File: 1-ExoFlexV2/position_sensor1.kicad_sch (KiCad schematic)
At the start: 28 parts, among them U51 SN74LVC1G08DBVR, U52 SN74LVC1G08DBVR, U53 SN74LVC3G14DCUT_V2

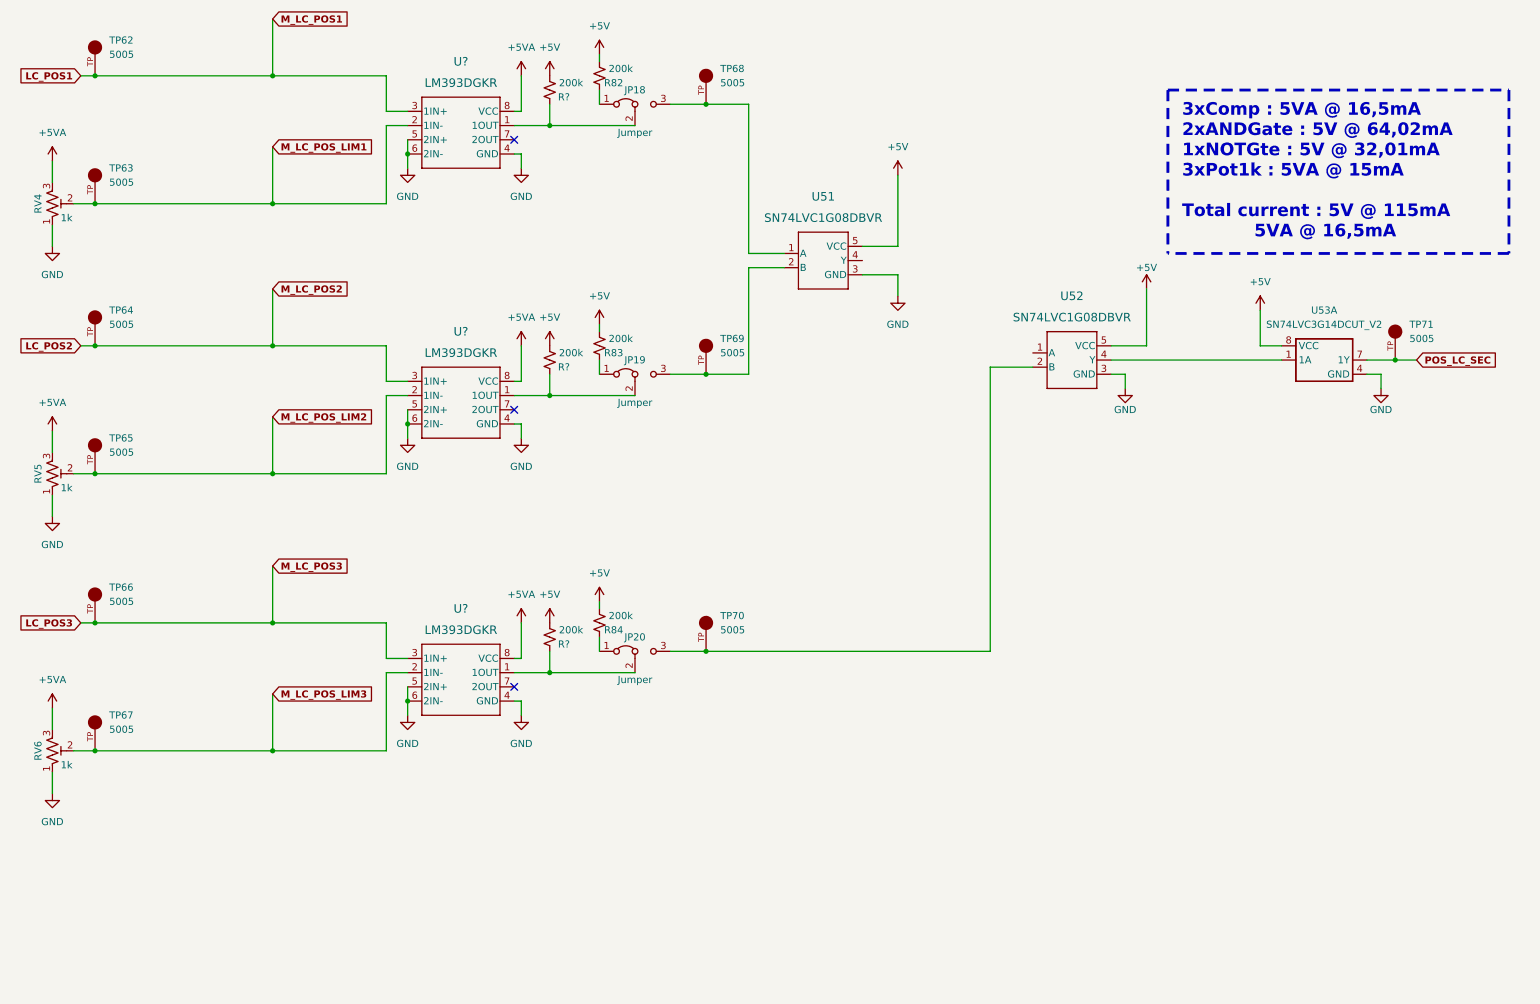
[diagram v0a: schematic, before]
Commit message: Chokes et RC
- Ajout des RF chokes
- Changement des résistance pour 0805
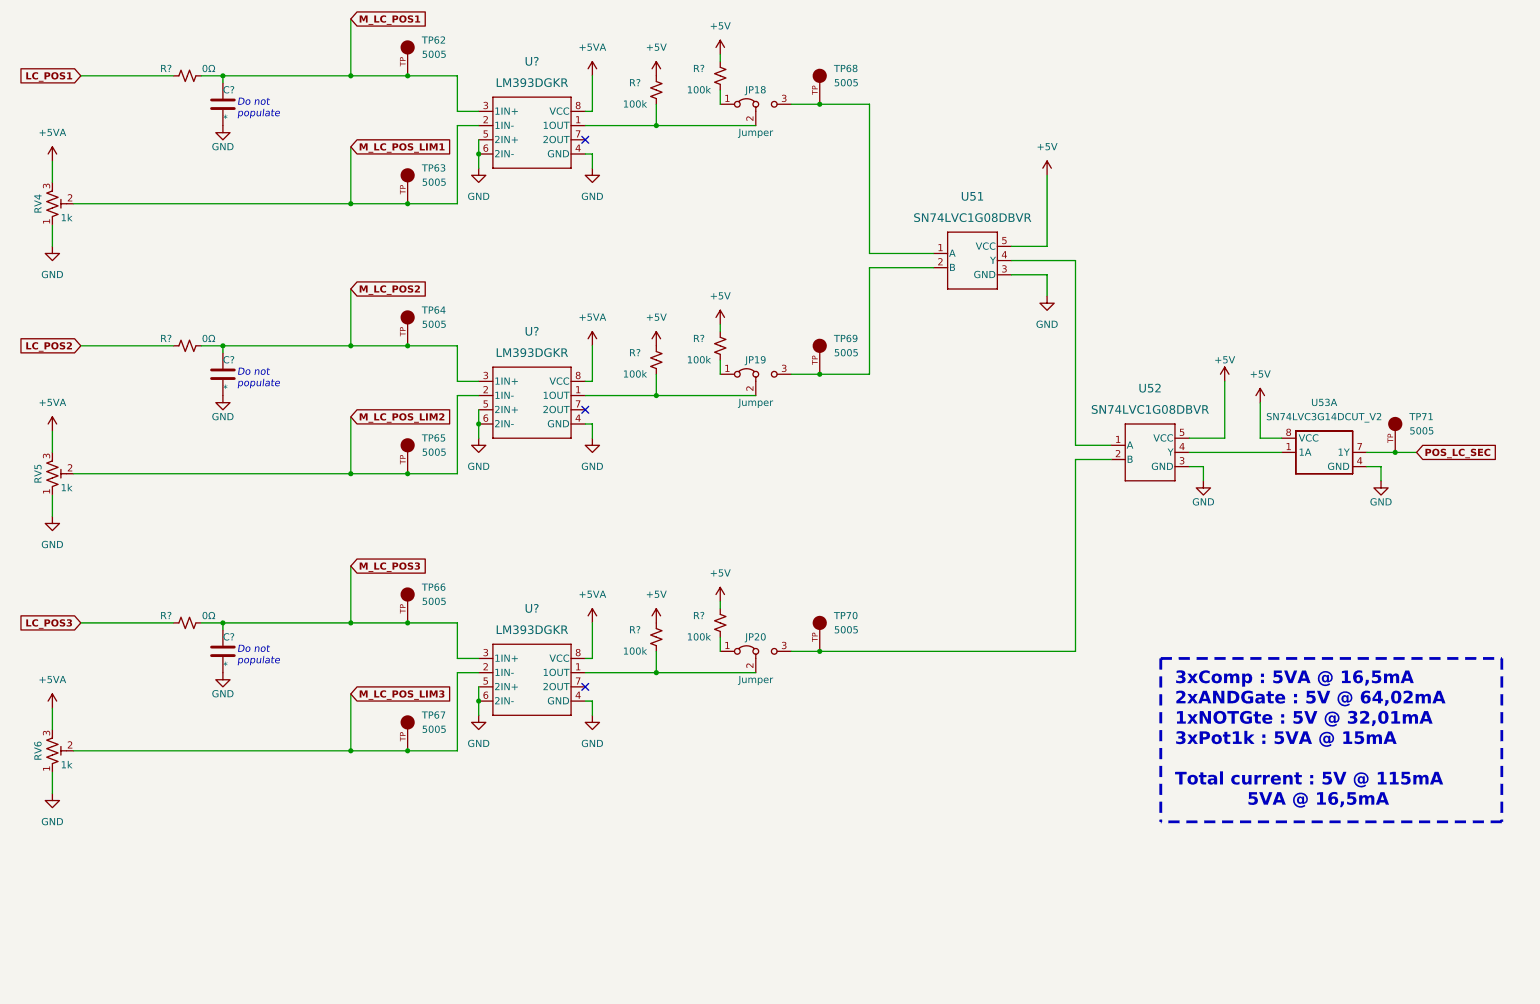
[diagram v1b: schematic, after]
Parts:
- removed R82, R83, R84, R? (x3): 200k, Resistor_SMD:R_0603_1608Metric, symbol Device:R_Small_US
- added C? (x3): *, Capacitor_SMD:C_0805_2012Metric, symbol Device:C
- added R? (x3): 0Ω, Resistor_SMD:R_0805_2012Metric, symbol Device:R_Small_US
- added R? (x6): 100k, Resistor_SMD:R_0805_2012Metric, symbol Device:R_Small_US
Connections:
- net +5V: now also R?.1, R?.1, R?.1, R?.1, R?.1, R?.1
- net GND: now also C?.2, C?.2, C?.2
- net LC_POS1: now also R?.1; no longer TP62.TP, U?.3 (1IN+)
- net LC_POS2: now also R?.1; no longer TP64.TP, U?.3 (1IN+)
- net LC_POS3: now also R?.1; no longer TP66.TP, U?.3 (1IN+)
- net at JP19.1 (A): now also R?.2
- net at JP19.2 (C), U?.1 (1OUT): now also R?.2
- net at JP18.2 (C), U?.1 (1OUT): now also R?.2
- net at JP20.2 (C), U?.1 (1OUT): now also R?.2
- net at U52.1 (A): now also U51.4 (Y)
- net at JP18.1 (A): now also R?.2
- net at JP20.1 (A): now also R?.2
- new net M_LC_POS1: C?.1, R?.2, TP62.TP, U?.3 (1IN+)
- new net M_LC_POS2: C?.1, R?.2, TP64.TP, U?.3 (1IN+)
- new net M_LC_POS3: C?.1, R?.2, TP66.TP, U?.3 (1IN+)
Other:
- note added: "Do not populate"
- moved on the sheet: JP18, JP19, JP20, TP62, TP63, TP64, TP65, TP66, TP67, TP68, TP69, TP70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

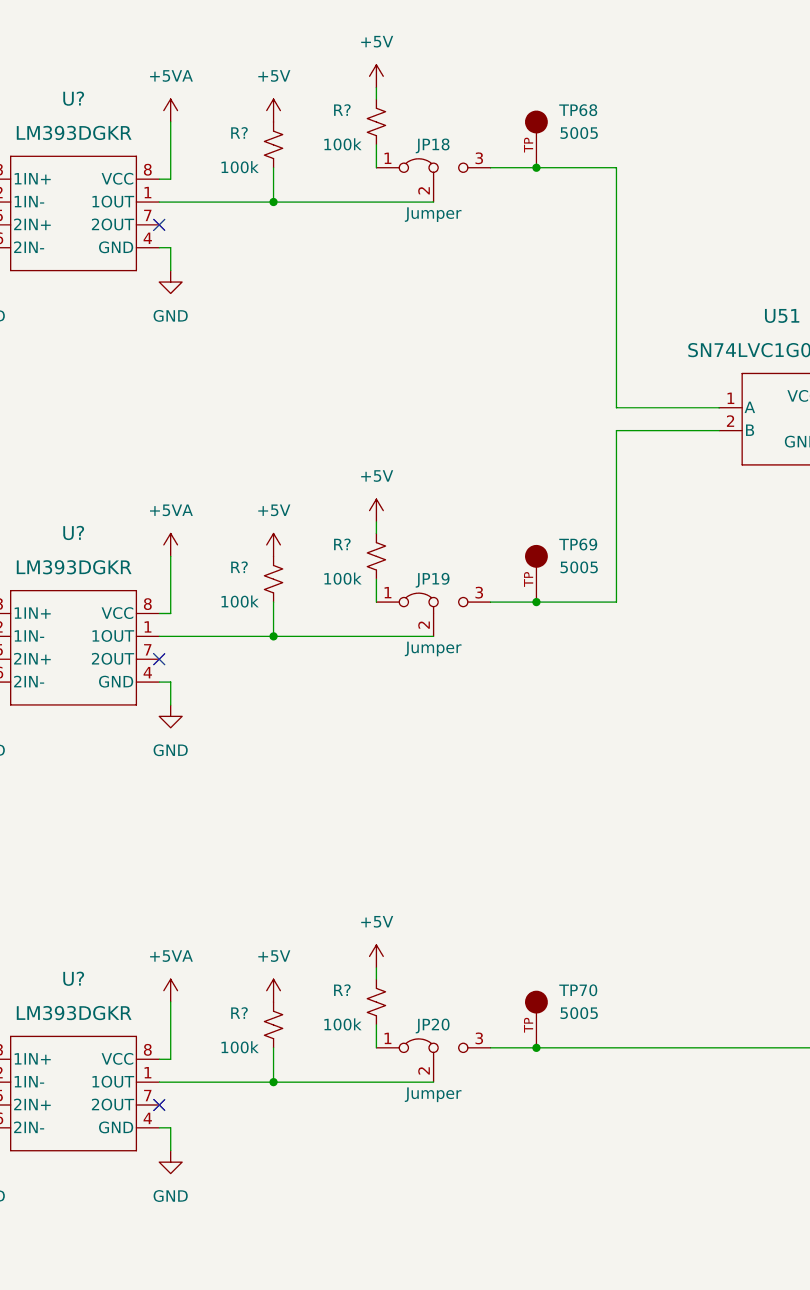
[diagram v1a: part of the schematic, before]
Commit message: Trimmer et jumper
-Changement de symbole de jumper
-Ajout des des trimmer aux endroits nécessaires
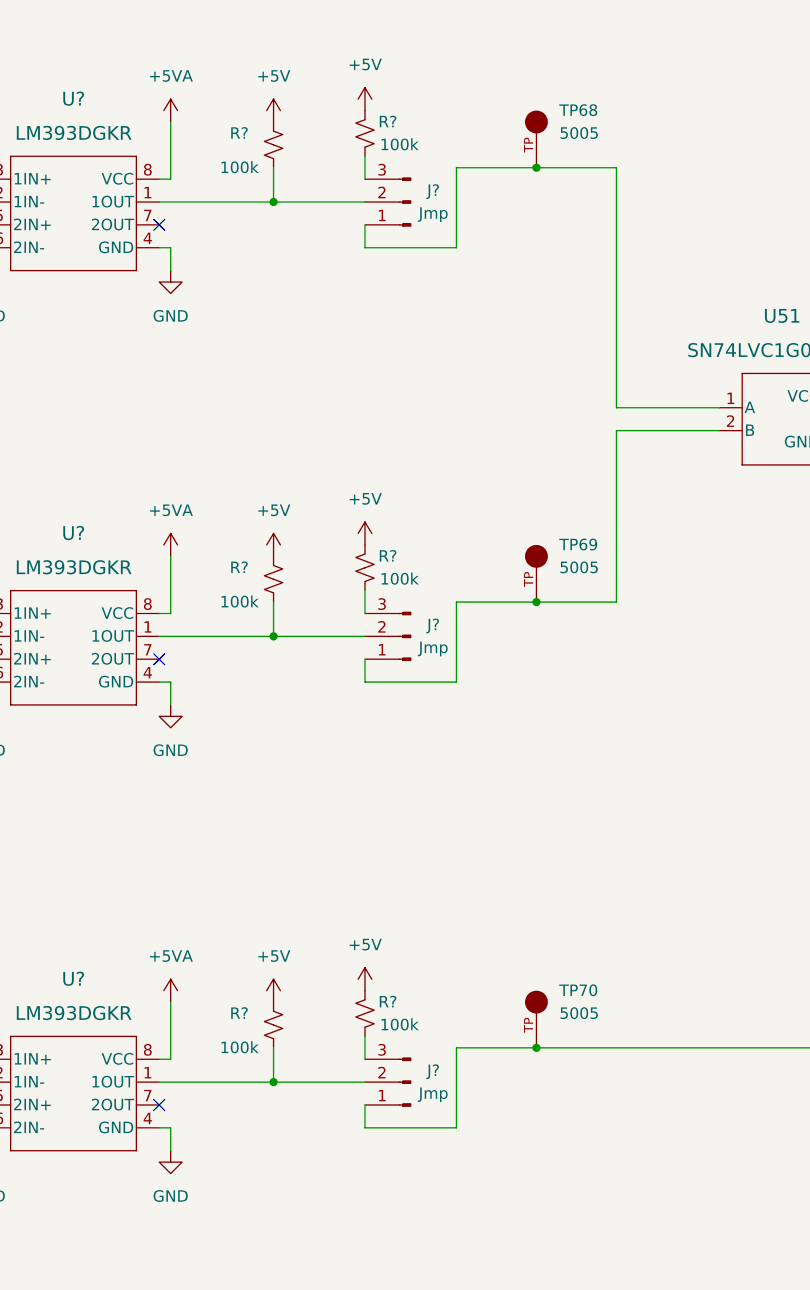
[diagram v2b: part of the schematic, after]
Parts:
- removed JP18, JP19, JP20: Jumper, Connector_PinHeader_2.54mm:PinHeader_1x03_P2.54mm_Vertical, symbol Jumper:Jumper_3_Bridged12
- removed R? (x3): 100k, Resistor_SMD:R_0805_2012Metric, symbol Device:R_Small_US
- added J? (x3): Jmp, symbol Connector:Conn_01x03_Male
- added R? (x3): 100k, Resistor_SMD:R_0805_2012Metric, symbol Device:R_Small_US
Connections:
- net +5V: now also R?.2, R?.2, R?.2
- net at R?.2, U?.1 (1OUT): now also J?.2 (Pin_2) (x3)
- net at TP69.TP, U51.2 (B): now also J?.1 (Pin_1)
- net at TP70.TP, U52.2 (B): now also J?.1 (Pin_1)
- net at TP68.TP, U51.1 (A): now also J?.1 (Pin_1)
- new net: J?.3 (Pin_3), R?.1 (x3)

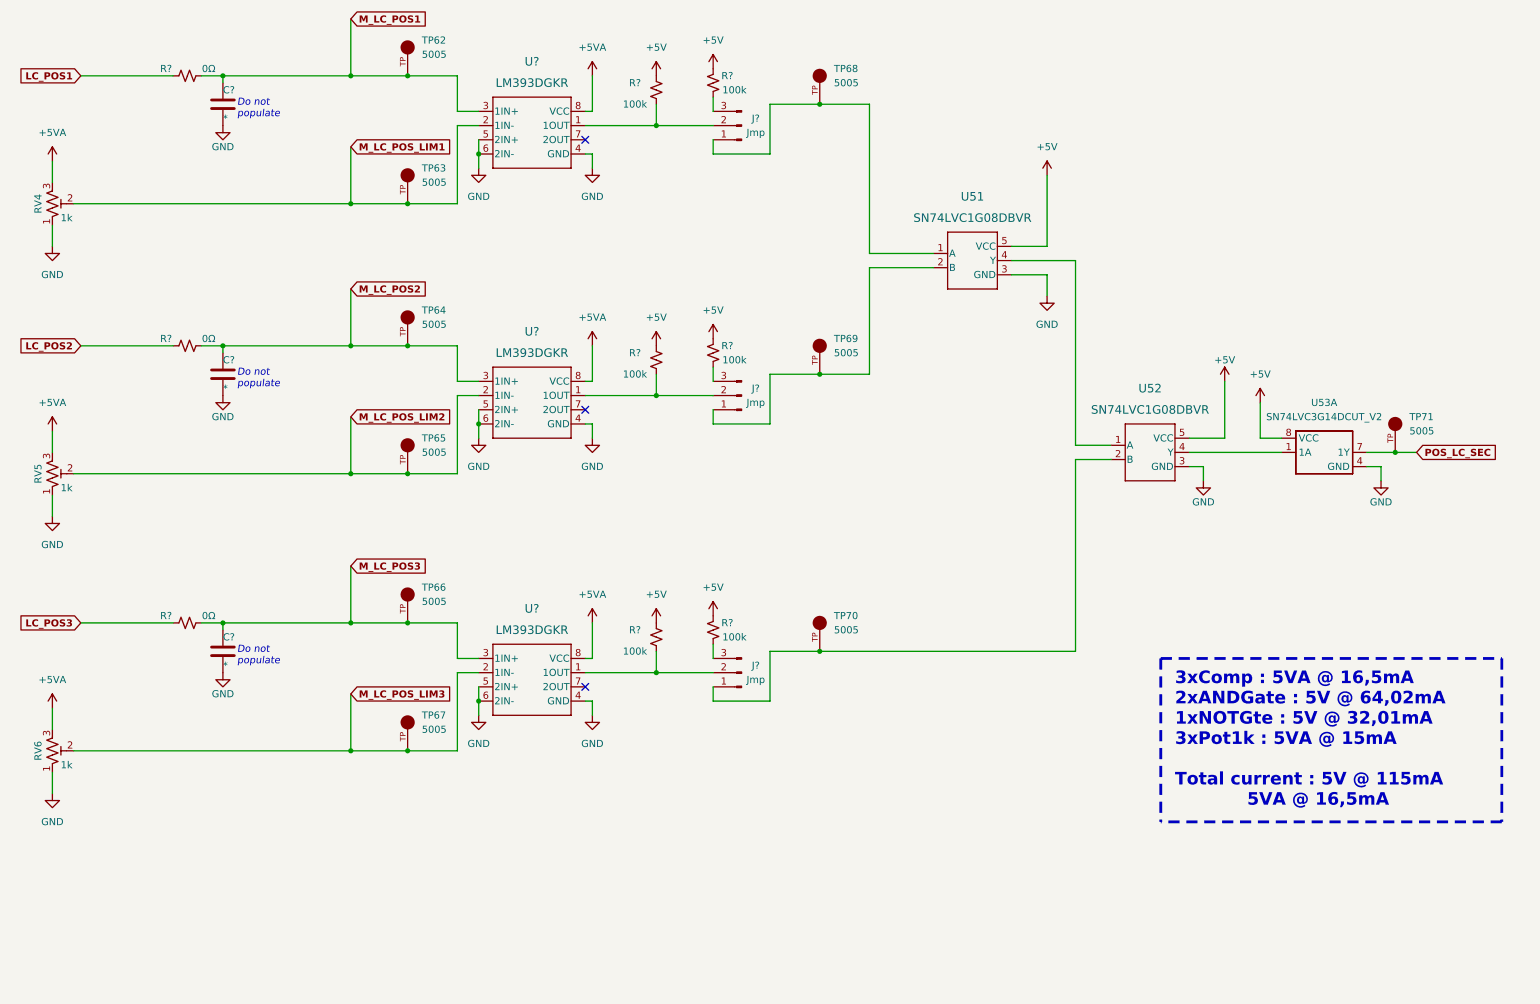
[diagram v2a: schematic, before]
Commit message: Test points et notes
- Ajout de tous les tests point nécessaires
-  Ajoute des sections de notes dans chaque page
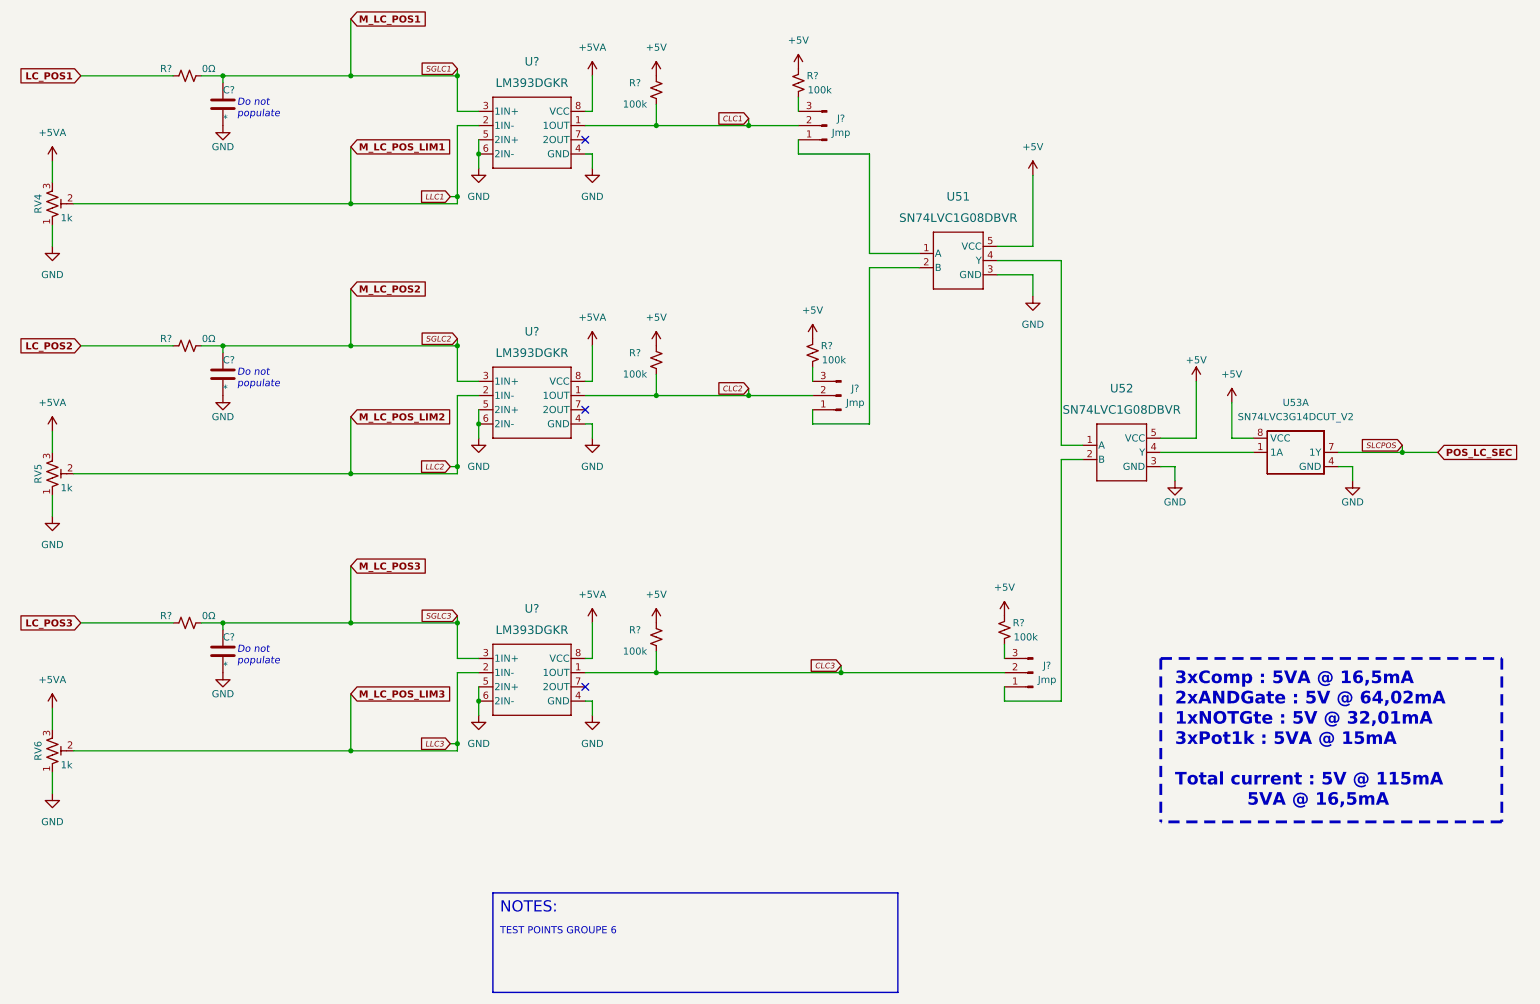
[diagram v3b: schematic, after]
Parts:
- removed TP62, TP63, TP64, TP65, TP66, TP67, TP68, TP69, TP70, TP71: 5005, FootPrint:KEYSTONE_5005, symbol SymLib:5005
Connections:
- net CLC1: now reaches J?.2 (Pin_2), R?.2, U?.1 (1OUT)
- net CLC3: now reaches J?.2 (Pin_2), R?.2, U?.1 (1OUT)
- net CLC2: now reaches J?.2 (Pin_2), R?.2, U?.1 (1OUT)
- net M_LC_POS_LIM1 renamed LLC1
- net M_LC_POS_LIM2 renamed LLC2
- net M_LC_POS_LIM3 renamed LLC3
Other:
- note added: "NOTES:"
- note added: "TEST POINTS GROUPE 6"
- moved on the sheet: J?, R?, U51, U52, U53A
